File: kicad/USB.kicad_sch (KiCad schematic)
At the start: 18 parts, among them J3 906-762B1026D10200, J4 906-762B1026D10200, U13 MT9700, U14 MT9700

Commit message: Change schematic and PCB
  changed component U11 from 8MBit to 32 MBit
  added qr-code on bottom overlay
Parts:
- removed C90, C92: 150 uF, Capacitor_Tantalum_SMD:CP_EIA-7343-31_Kemet-D, symbol -- database:Capacitors/CAP_TPSD157M016R0150
- added C90, C92: 150 uF, Capacitor_Tantalum_SMD:CP_EIA-7343-31_Kemet-D, symbol db:Capacitors/CAP_TAJD157K010RNJ
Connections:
- net GNDREF: now also C90.2, C92.2
- net USB1_VBUS: now also C92.1
- net USB2_VBUS: now also C90.1

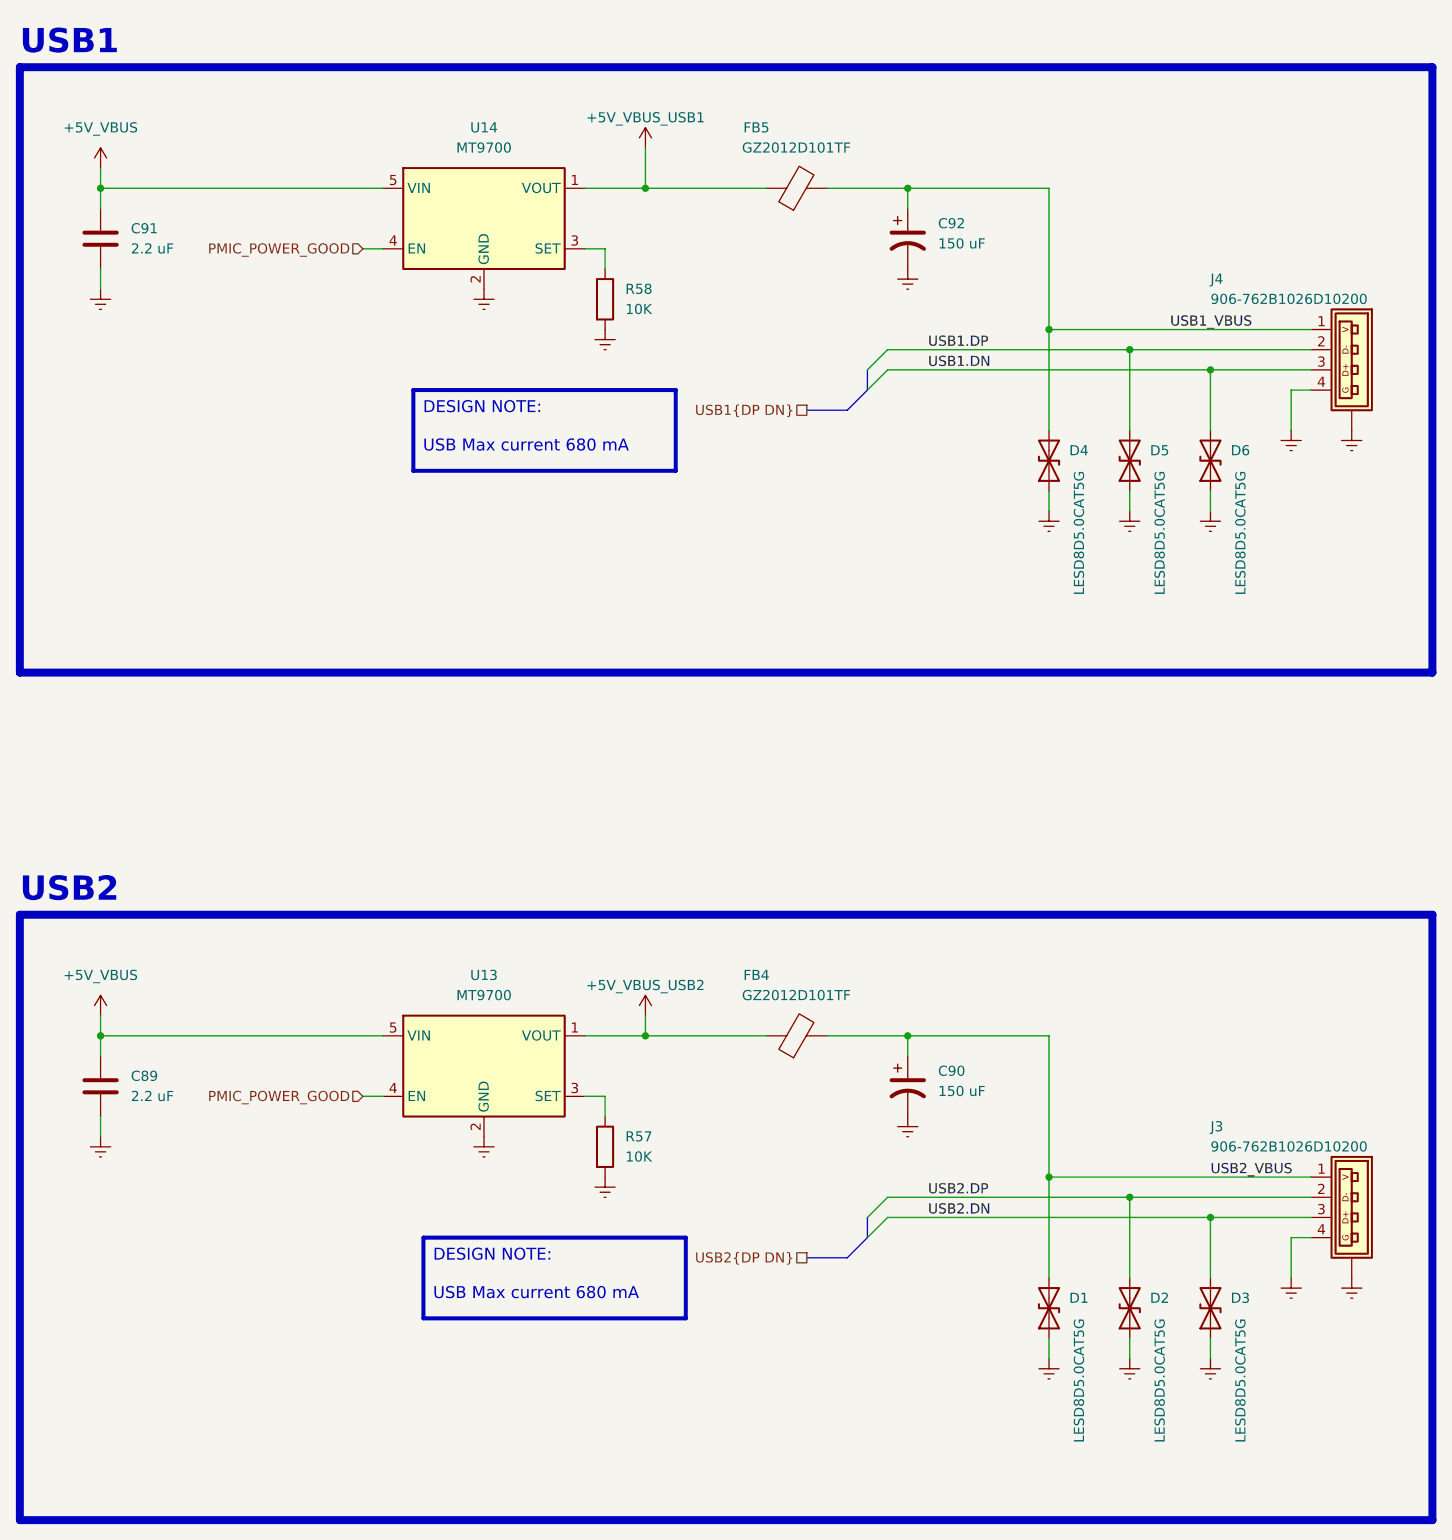
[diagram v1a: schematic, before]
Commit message: Fix hardware bugs - Fix part number in bom for resistors R103, R113, R114, R118 -> 680K - Fix part number in BOM for resistors R13, R16 -> 68K - Fix part number in BOM for resistor R14 -> 4.7K - Fix part number in BOM for capacitors C100, C101, C12, C13, C130, C131, C133, C135, C140, C141, C15, C19, C57, C58, C7, C99 -> 100nF - Fix footprint for USB-A connectors - Fix power buttom pull-up resistor connection -> connect to +3.3V_STAND_BY
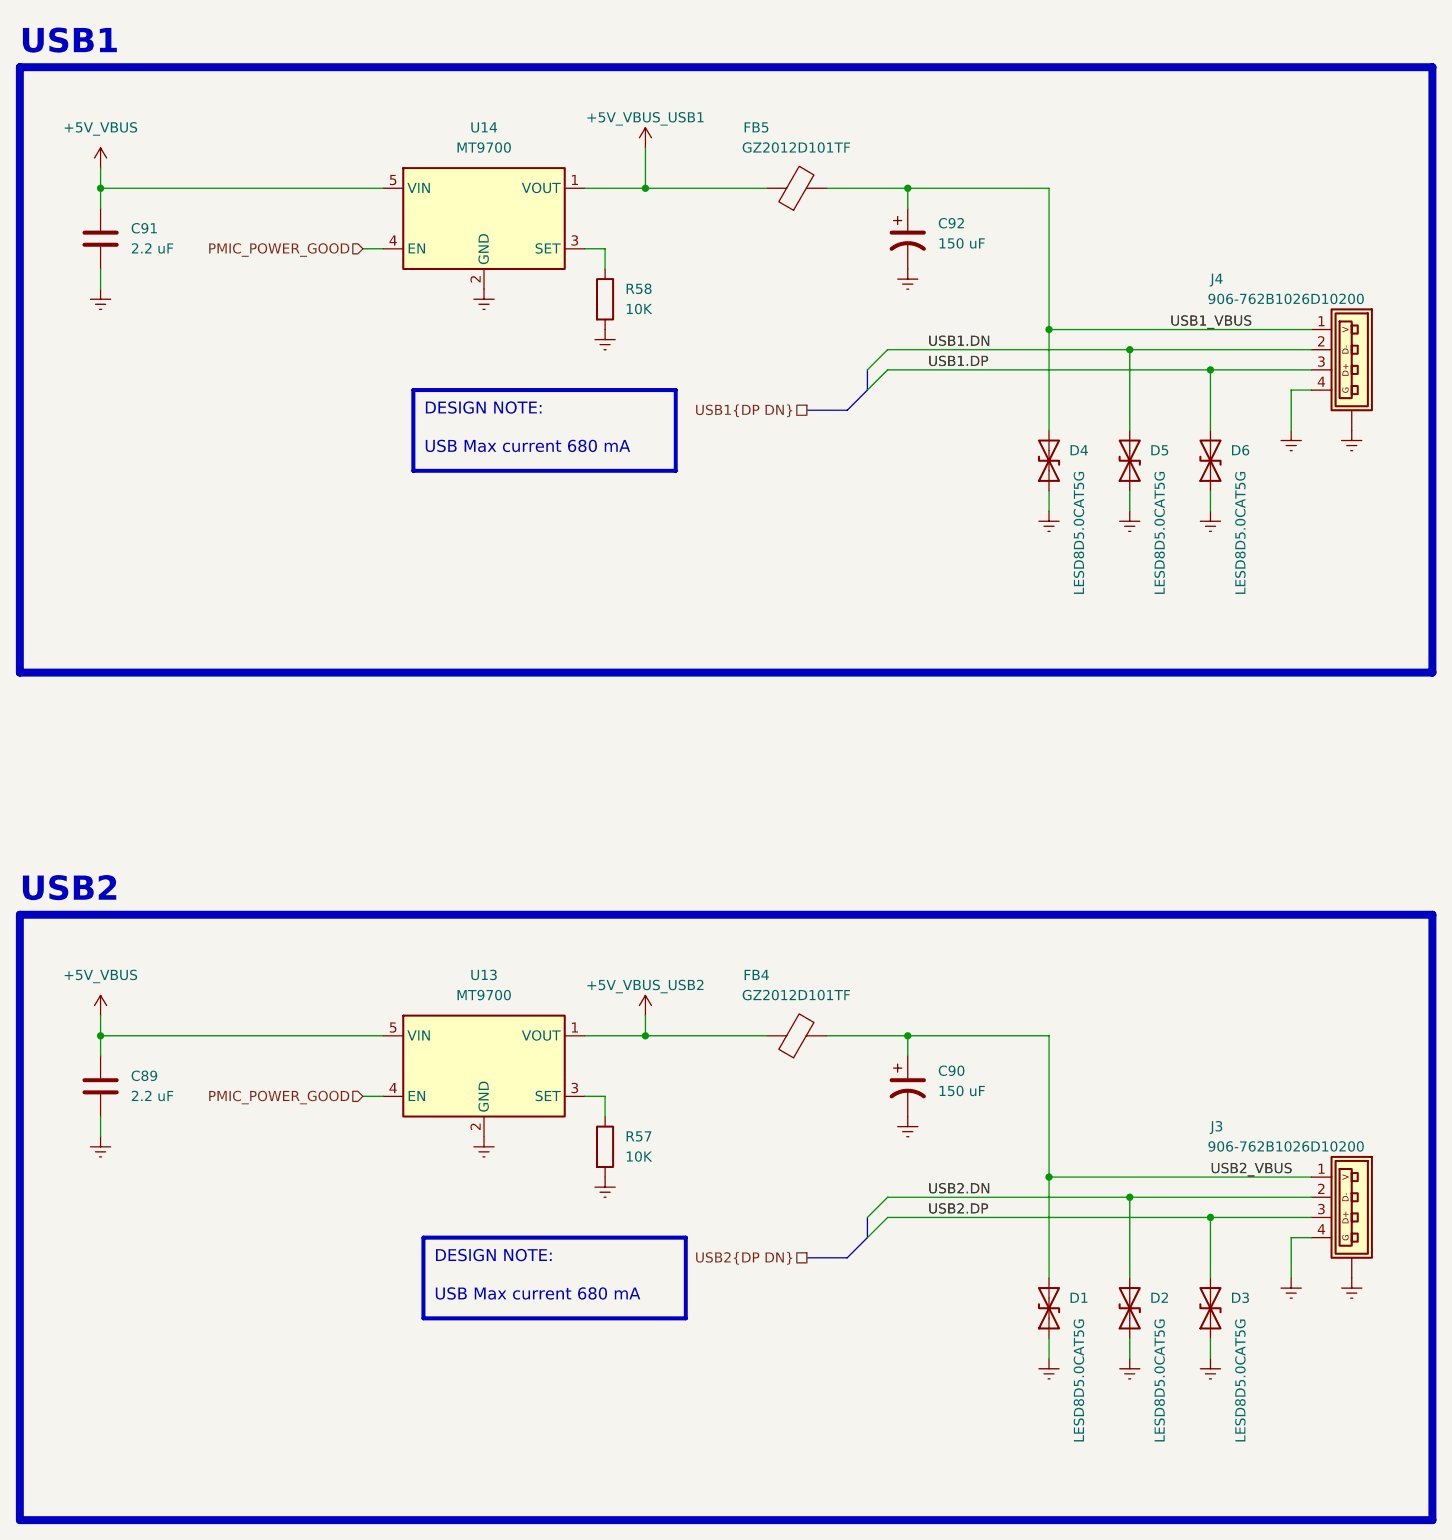
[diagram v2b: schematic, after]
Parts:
- J3, J4: symbol -- database:Mechanical/USB-A_906-762B1026D10200 -> ts_database:Mechanical/USB-A_906-762B1026D10200
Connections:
- net USB1.DN: now also D5.2 (A2), J4.2 (D-); no longer D6.2 (A2), J4.3 (D+)
- net USB1.DP: now also D6.2 (A2), J4.3 (D+); no longer D5.2 (A2), J4.2 (D-)
- net USB2.DN: now also D2.2 (A2), J3.2 (D-); no longer D3.2 (A2), J3.3 (D+)
- net USB2.DP: now also D3.2 (A2), J3.3 (D+); no longer D2.2 (A2), J3.2 (D-)
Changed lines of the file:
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@@
 (kicad_sch
-	(version 20231120)
+	(version 20250114)
 	(generator "eeschema")
-	(generator_version "8.0")
+	(generator_version "9.0")
 	(paper "A3")
 	(title_block
 		(title "i.MX6 Demo Board")
-		(date "2024-05-26")
-		(rev "00")
+		(date "2026-02-16")
+		(rev "01")
 		(company "ts-manuel")
 	)
+	(rectangle
+		(start 116.84 162.56)
+		(end 294.64 238.76)
+		(stroke
+			(width 1)
+			(type default)
+		)
+		(fill
+			(type none)
+		)
+	)
+	(rectangle
+		(start 116.84 55.88)
+		(end 294.64 132.08)
+		(stroke
+			(width 1)
+			(type default)
+		)
+		(fill
+			(type none)
+		)
+	)
+	(text "USB1"
+		(exclude_from_sim no)
+		(at 116.84 54.61 0)
+		(effects
+			(font
+				(size 3.048 3.048)
+				(bold yes)
+			)
+			(justify left bottom)
+		)
+	)
+	(text "USB2"
+		(exclude_from_sim no)
+		(at 116.84 161.29 0)
+		(effects
+			(font
+				(size 3.048 3.048)
+				(bold yes)
+			)
+			(justify left bottom)
+		)
+	)
+	(text_box "DESIGN NOTE:\n\nUSB Max current 680 mA"
+		(exclude_from_sim no)
+		(at 167.64 203.2 0)
+		(size 33.02 10.16)
+		(margins 1.375 1.375 1.375 1.375)
+		(stroke
+			(width 0.5)
+			(type default)
+			(color 255 229 153 1)
+		)
+		(fill
+			(type color)
+			(color 243 243 243 1)
+		)
+		(effects
+			(font
+				(size 1.5 1.5)
+			)
+			(justify left top)
+		)
+	)
+	(text_box "DESIGN NOTE:\n\nUSB Max current 680 mA"
+		(exclude_from_sim no)
+		(at 166.37 96.52 0)
+		(size 33.02 10.16)
+		(margins 1.375 1.375 1.375 1.375)
+		(stroke
+			(width 0.5)
+			(type default)
+			(color 255 229 153 1)
+		)
+		(fill
+			(type color)
+			(color 243 243 243 1)
+		)
+		(effects
+			(font
+				(size 1.5 1.5)
+			)
+			(justify left top)
+		)
+	)
 	(junction
 		(at 256.54 91.44)
@@
 	(wire
 		(pts
-			(xy 226.06 91.44) (xy 256.54 91.44)
-		)
-		(stroke
-			(width 0)
-			(type default)
-		)
-	)
-	(wire
-		(pts
 			(xy 190.5 185.42) (xy 190.5 187.96)
 		)
@@
 	(wire
 		(pts
-			(xy 226.06 93.98) (xy 266.7 93.98)
-		)
-		(stroke
-			(width 0)
-			(type default)
-		)
-	)
-	(wire
-		(pts
 			(xy 127 71.12) (xy 162.56 71.12)
 		)
@@
 	(wire
 		(pts
+			(xy 226.06 198.12) (xy 256.54 198.12)
+		)
+		(stroke
+			(width 0)
+			(type default)
+		)
+	)
+	(wire
+		(pts
 			(xy 218.44 71.12) (xy 228.6 71.12)
 		)
@@
 	(wire
 		(pts
+			(xy 226.06 91.44) (xy 256.54 91.44)
+		)
+		(stroke
+			(width 0)
+			(type default)
+		)
+	)
+	(wire
+		(pts
 			(xy 246.38 88.9) (xy 279.4 88.9)
 		)
@@
 	(wire
 		(pts
-			(xy 226.06 198.12) (xy 256.54 198.12)
+			(xy 226.06 93.98) (xy 266.7 93.98)
 		)
 		(stroke
@@
 		)
 	)
-	(rectangle
-		(start 116.84 162.56)
-		(end 294.64 238.76)
-		(stroke
-			(width 1)
-			(type default)
-		)
-		(fill
-			(type none)
-		)
-	)
-	(rectangle
-		(start 116.84 55.88)
-		(end 294.64 132.08)
-		(stroke
-			(width 1)
-			(type default)
-		)
-		(fill
-			(type none)
-		)
-	)
-	(text_box "DESIGN NOTE:\n\nUSB Max current 680 mA"
-		(exclude_from_sim no)
-		(at 167.64 203.2 0)
-		(size 33.02 10.16)
-		(stroke
-			(width 0.5)
-			(type default)
-			(color 255 229 153 1)
-		)
-		(fill
-			(type color)
-			(color 243 243 243 1)
-		)
-		(effects
-			(font
-				(size 1.5 1.5)
-			)
-			(justify left top)
-		)
-	)
-	(text_box "DESIGN NOTE:\n\nUSB Max current 680 mA"
-		(exclude_from_sim no)
-		(at 166.37 96.52 0)
-		(size 33.02 10.16)
-		(stroke
-			(width 0.5)
-			(type default)
-			(color 255 229 153 1)
-		)
-		(fill
-			(type color)
-			(color 243 243 243 1)
-		)
-		(effects
-			(font
-				(size 1.5 1.5)
-			)
-			(justify left top)
-		)
-	)
-	(text "USB1"
-		(exclude_from_sim no)
-		(at 116.84 54.61 0)
-		(effects
-			(font
-				(size 3.048 3.048)
-				(bold yes)
-			)
-			(justify left bottom)
-		)
-	)
-	(text "USB2"
-		(exclude_from_sim no)
-		(at 116.84 161.29 0)
-		(effects
-			(font
-				(size 3.048 3.048)
-				(bold yes)
-			)
-			(justify left bottom)
-		)
-	)
 	(label "USB1.DP"
-		(at 231.14 91.44 0)
-		(fields_autoplaced yes)
+		(at 231.14 93.98 0)
 		(effects
 			(font
@@
 	(label "USB2_VBUS"
 		(at 266.7 195.58 0)
-		(fields_autoplaced yes)
 		(effects
 			(font
@@
 	(label "USB1_VBUS"
 		(at 261.62 88.9 0)
-		(fields_autoplaced yes)
 		(effects
 			(font
@@
 	)
 	(label "USB1.DN"
-		(at 231.14 93.98 0)
-		(fields_autoplaced yes)
+		(at 231.14 91.44 0)
 		(effects
 			(font
@@
 	)
 	(label "USB2.DN"
-		(at 231.14 200.66 0)
-		(fields_autoplaced yes)
+		(at 231.14 198.12 0)
 		(effects
 			(font
@@
 	)
 	(label "USB2.DP"
-		(at 231.14 198.12 0)
-		(fields_autoplaced yes)
+		(at 231.14 200.66 0)
 		(effects
 			(font
@@
 		(shape input)
 		(at 160.02 78.74 180)
-		(fields_autoplaced yes)
 		(effects
 			(font
@@
 		(shape input)
 		(at 160.02 185.42 180)
-		(fields_autoplaced yes)
 		(effects
 			(font
@@
 		(shape passive)
 		(at 215.9 99.06 180)
-		(fields_autoplaced yes)
 		(effects
 			(font
@@
 		(shape passive)
 		(at 215.9 205.74 180)
-		(fields_autoplaced yes)
 		(effects
 			(font
@@
 	)
 	(symbol
-		(lib_id "-- database:Mechanical/USB-A_906-762B1026D10200")
+		(lib_id "ts_database:Mechanical/USB-A_906-762B1026D10200")
 		(at 287.02 86.36 0)
 		(mirror y)
@@
 		)
 		(property "Value" "906-762B1026D10200"
-			(at 266.7 85.09 0)
+			(at 276.225 85.09 0)
 			(effects
 				(font
 					(size 1.27 1.27)
 				)
-				(justify right)
 			)
 		)
@@
 	)
 	(symbol
-		(lib_id "-- database:Mechanical/USB-A_906-762B1026D10200")
+		(lib_id "ts_database:Mechanical/USB-A_906-762B1026D10200")
 		(at 287.02 193.04 0)
 		(mirror y)
@@
 		)
 		(property "Value" "906-762B1026D10200"
-			(at 266.7 191.77 0)
+			(at 276.225 191.77 0)
 			(effects
 				(font
 					(size 1.27 1.27)
 				)
-				(justify right)
 			)
 		)
